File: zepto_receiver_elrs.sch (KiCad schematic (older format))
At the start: 44 parts, among them J1 u.fl, SW1 SW_Push, U1 STM32WLE5JBI6, U2 NCP160, U3 BGS12PL6E6327XTSA1

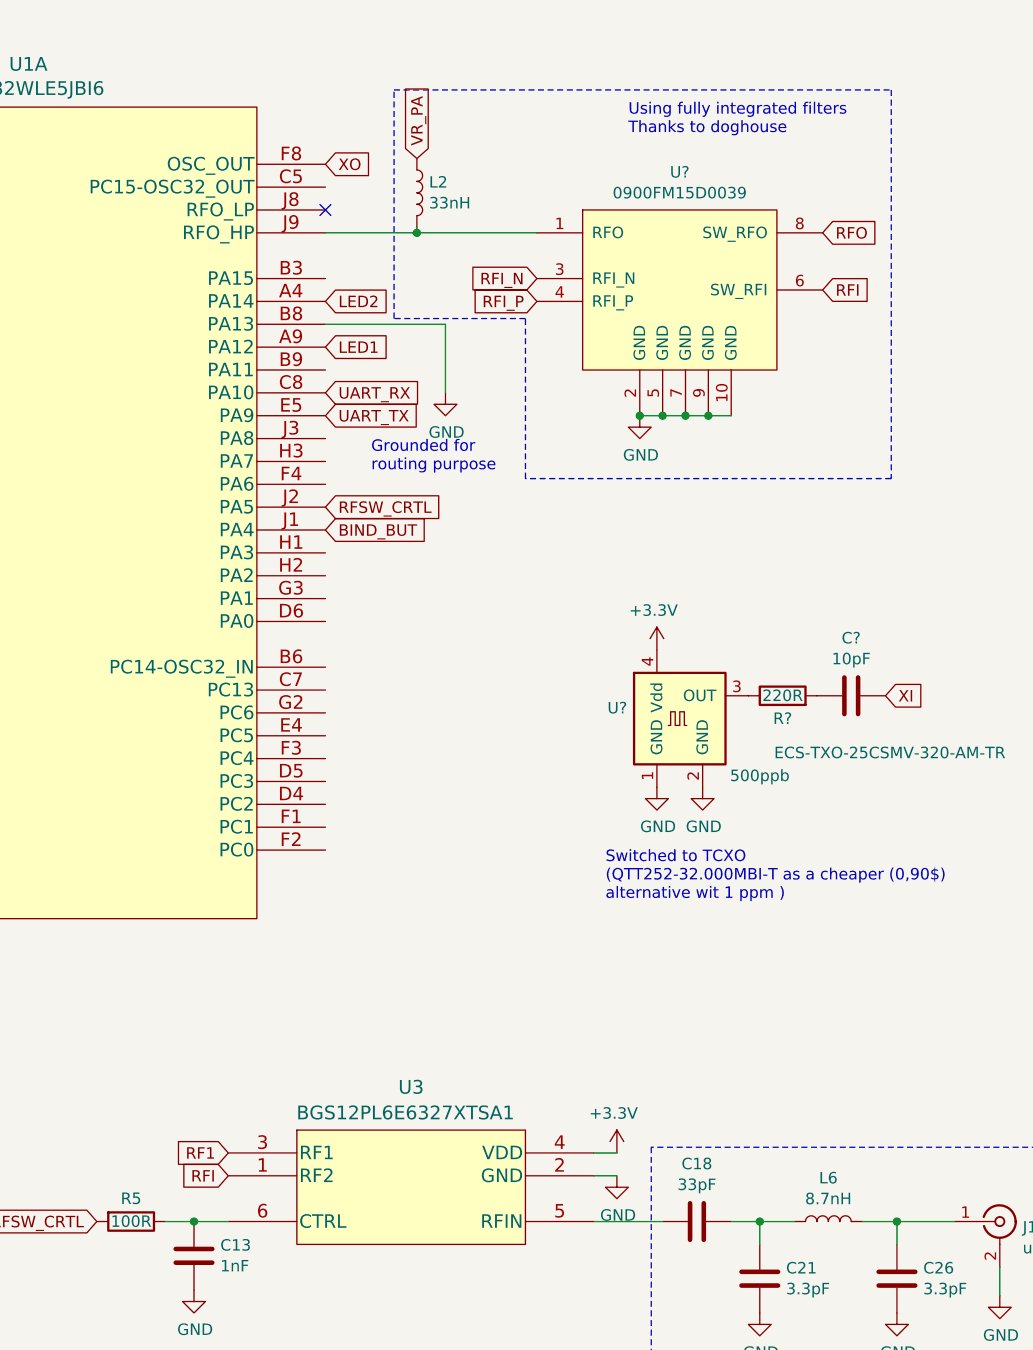
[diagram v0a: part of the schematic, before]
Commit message: new layout with integrated passives and TCXO
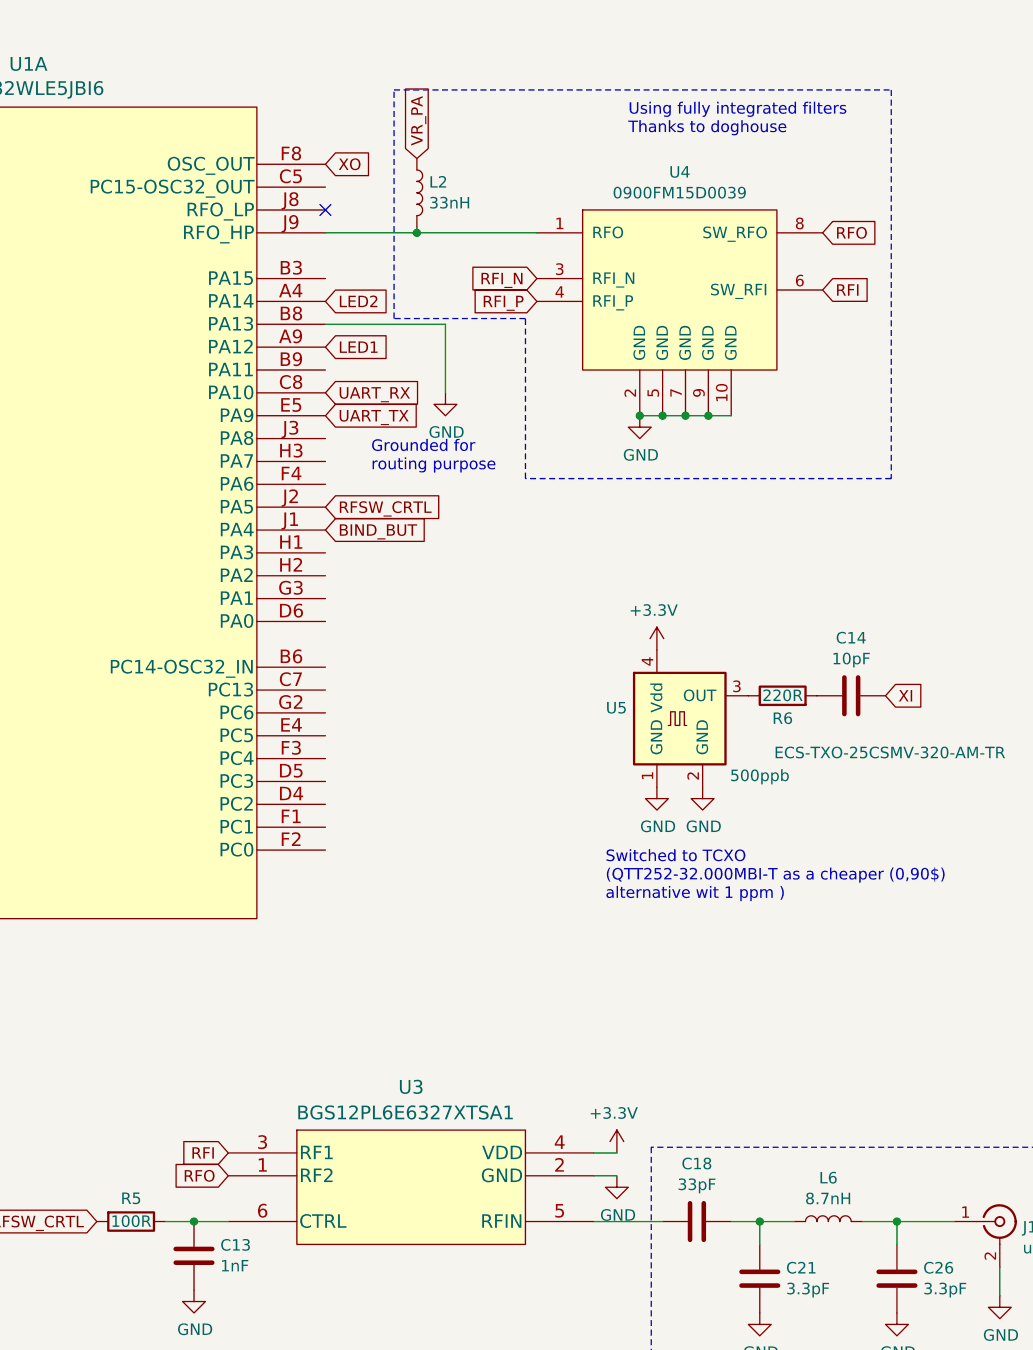
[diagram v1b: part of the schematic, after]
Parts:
- gave numbers to parts that had none: 4
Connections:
- net RF1 is gone; now on net RFI: U3.3 (RF1)
- net RFI: no longer U3.1 (RF2)
- net RFO: now also U3.1 (RF2)
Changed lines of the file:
@@
 EESchema Schematic File Version 4
-LIBS:zepto_receiver_elrs-cache
 EELAYER 30 0
 EELAYER END
@@
 	8400 1350 8400 1325
 Text GLabel 7575 5375 0    50   Input ~ 0
-RF1
-Text GLabel 7575 5475 0    50   Input ~ 0
 RFI
 $Comp
@@
 $EndComp
 $Comp
-L sch_comp:0900FM15D0039 U?
+L sch_comp:0900FM15D0039 U4
 U 1 1 604AB514
 P 9575 1600
-F 0 "U?" H 9550 2115 50  0000 C CNN
+F 0 "U4" H 9550 2115 50  0000 C CNN
 F 1 "0900FM15D0039" H 9550 2024 50  0000 C CNN
 F 2 "ftprnts:0900FM15D0039" H 9575 1600 50  0001 C CNN
@@
 Connection ~ 8400 1350
 $Comp
-L power:GND #PWR?
+L power:GND #PWR0102
 U 1 1 604BECC8
 P 9375 2150
-F 0 "#PWR?" H 9375 1900 50  0001 C CNN
+F 0 "#PWR0102" H 9375 1900 50  0001 C CNN
 F 1 "GND" H 9380 1977 50  0000 C CNN
 F 2 "" H 9375 2150 50  0001 C CNN
@@
 	9675 2150 9575 2150
 $Comp
-L sch_comp:ECS-TXO-25CSMV U?
+L sch_comp:ECS-TXO-25CSMV U5
 U 1 1 604C7152
 P 9550 3475
-F 0 "U?" H 9320 3521 50  0000 R CNN
+F 0 "U5" H 9320 3521 50  0000 R CNN
 F 1 "ECS-TXO-25CSMV-320-AM-TR" H 10975 3325 50  0000 R CNN
 F 2 "Crystal:Crystal_SMD_2520-4Pin_2.5x2.0mm" H 10250 3025 50  0001 C CNN
@@
 $EndComp
 $Comp
-L Device:C C?
+L Device:C C14
 U 1 1 604C890B
 P 10300 3375
-F 0 "C?" V 10552 3375 50  0000 C CNN
+F 0 "C14" V 10552 3375 50  0000 C CNN
 F 1 "10pF" V 10461 3375 50  0000 C CNN
 F 2 "ftprnts:C_0201_0603Metric_dense" H 10338 3225 50  0001 C CNN
@@
 $EndComp
 $Comp
-L Device:R R?
+L Device:R R6
 U 1 1 604C9485
 P 10000 3375
-F 0 "R?" V 9900 3375 50  0000 C CNN
+F 0 "R6" V 9900 3375 50  0000 C CNN
 F 1 "220R" V 10000 3375 50  0000 C CNN
 F 2 "ftprnts:R_0201_0603Metric_dense" V 9930 3375 50  0001 C CNN
@@
 XI
 $Comp
-L power:GND #PWR?
+L power:GND #PWR0103
 U 1 1 604CCBA0
 P 9450 3775
-F 0 "#PWR?" H 9450 3525 50  0001 C CNN
+F 0 "#PWR0103" H 9450 3525 50  0001 C CNN
 F 1 "GND" H 9455 3602 50  0000 C CNN
 F 2 "" H 9450 3775 50  0001 C CNN
@@
 $EndComp
 $Comp
-L power:GND #PWR?
+L power:GND #PWR0104
 U 1 1 604CD2CB
 P 9650 3775
-F 0 "#PWR?" H 9650 3525 50  0001 C CNN
+F 0 "#PWR0104" H 9650 3525 50  0001 C CNN
 F 1 "GND" H 9655 3602 50  0000 C CNN
 F 2 "" H 9650 3775 50  0001 C CNN
@@
 $EndComp
 $Comp
-L power:+3.3V #PWR?
+L power:+3.3V #PWR0105
 U 1 1 604CD48E
 P 9450 3175
-F 0 "#PWR?" H 9450 3025 50  0001 C CNN
+F 0 "#PWR0105" H 9450 3025 50  0001 C CNN
 F 1 "+3.3V" H 9465 3348 50  0000 C CNN
 F 2 "" H 9450 3175 50  0001 C CNN
@@
 Text Notes 4400 7650 0    50   ~ 0
 Tantal and thes capacitors form together with the layerstack\na complex dcoupling system. They are all needed
+Text GLabel 7575 5475 0    50   Input ~ 0
+RFO
 $EndSCHEMATC
